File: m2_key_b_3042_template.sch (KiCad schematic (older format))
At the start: 4 parts, among them J1 M.2_Key_B

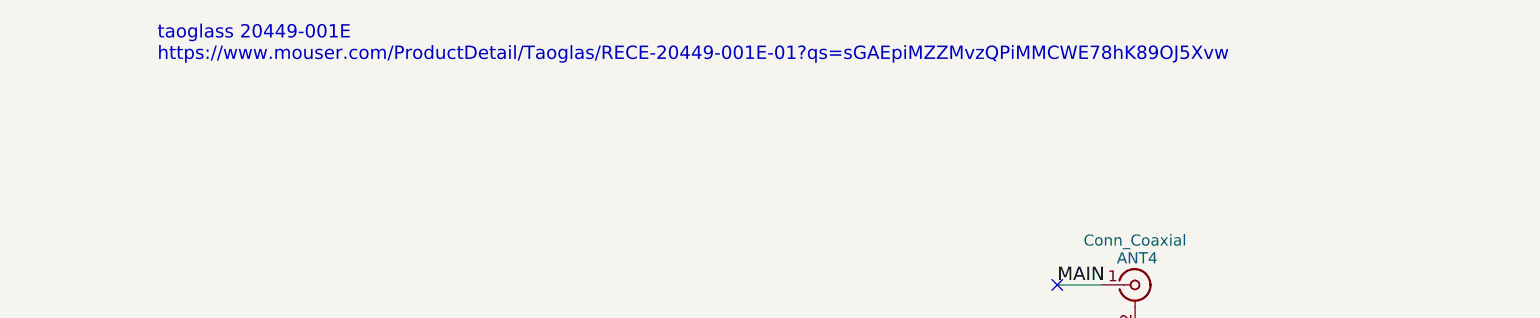
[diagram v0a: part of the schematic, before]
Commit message: Add MHF4 datasheet to the field values and remove the text reference
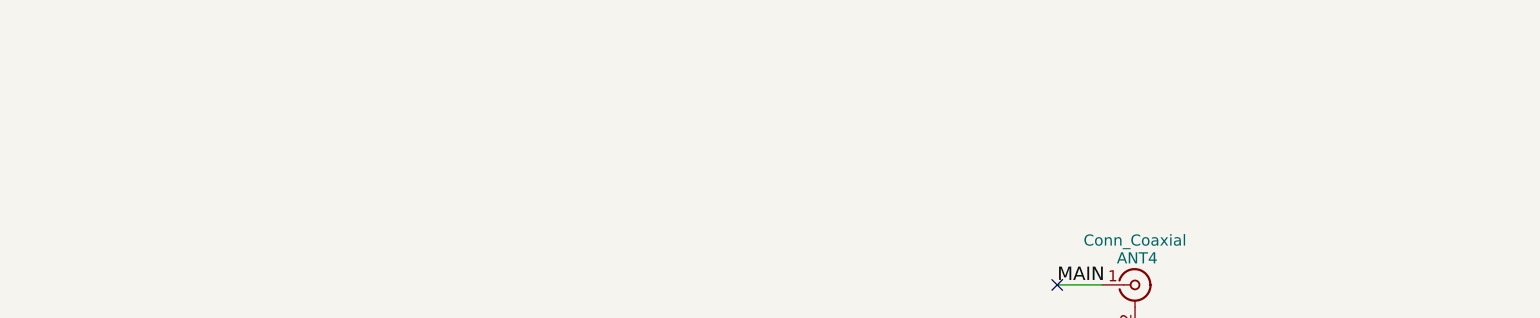
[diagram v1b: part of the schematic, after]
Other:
- note removed: "taoglass 20449-001E\nhttps://www.mouser.com/ProductDetail/Taoglas/RECE-20449-001E-01?qs=sGAEpiMZZMvzQPiMMCWE78hK89OJ5Xvw"
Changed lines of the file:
@@
 Wire Wire Line
 	4850 5400 4850 5350
-Text Notes 5750 950  0    60   ~ 0
-taoglass 20449-001E\nhttps://www.mouser.com/ProductDetail/Taoglas/RECE-20449-001E-01?qs=sGAEpiMZZMvzQPiMMCWE78hK89OJ5Xvw
 $Comp
 L Conn_Coaxial ANT1
@@
 F 1 "Conn_Coaxial" H 10150 3800 50  0000 C CNN
 F 2 "m2_key_b_3042:MHF4_20449-001E" H 10150 3600 50  0001 C CNN
-F 3 "" H 10150 3600 50  0001 C CNN
+F 3 "https://www.mouser.com/ds/2/398/RECE.20449.001E.01-27117.pdf" H 10150 3600 50  0001 C CNN
 	1    10150 3600
 	1    0    0    -1
@@
 F 1 "Conn_Coaxial" H 10150 3050 50  0000 C CNN
 F 2 "m2_key_b_3042:MHF4_20449-001E" H 10150 2850 50  0001 C CNN
-F 3 "" H 10150 2850 50  0001 C CNN
+F 3 "https://www.mouser.com/ds/2/398/RECE.20449.001E.01-27117.pdf" H 10150 2850 50  0001 C CNN
 	1    10150 2850
 	1    0    0    -1
@@
 F 1 "Conn_Coaxial" H 10150 2150 50  0000 C CNN
 F 2 "m2_key_b_3042:MHF4_20449-001E" H 10150 1950 50  0001 C CNN
-F 3 "" H 10150 1950 50  0001 C CNN
+F 3 "https://www.mouser.com/ds/2/398/RECE.20449.001E.01-27117.pdf" H 10150 1950 50  0001 C CNN
 	1    10150 1950
 	1    0    0    -1
